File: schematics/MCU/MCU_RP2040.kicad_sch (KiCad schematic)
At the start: 34 parts, among them X1 ECS-2520MVLC-120-CN

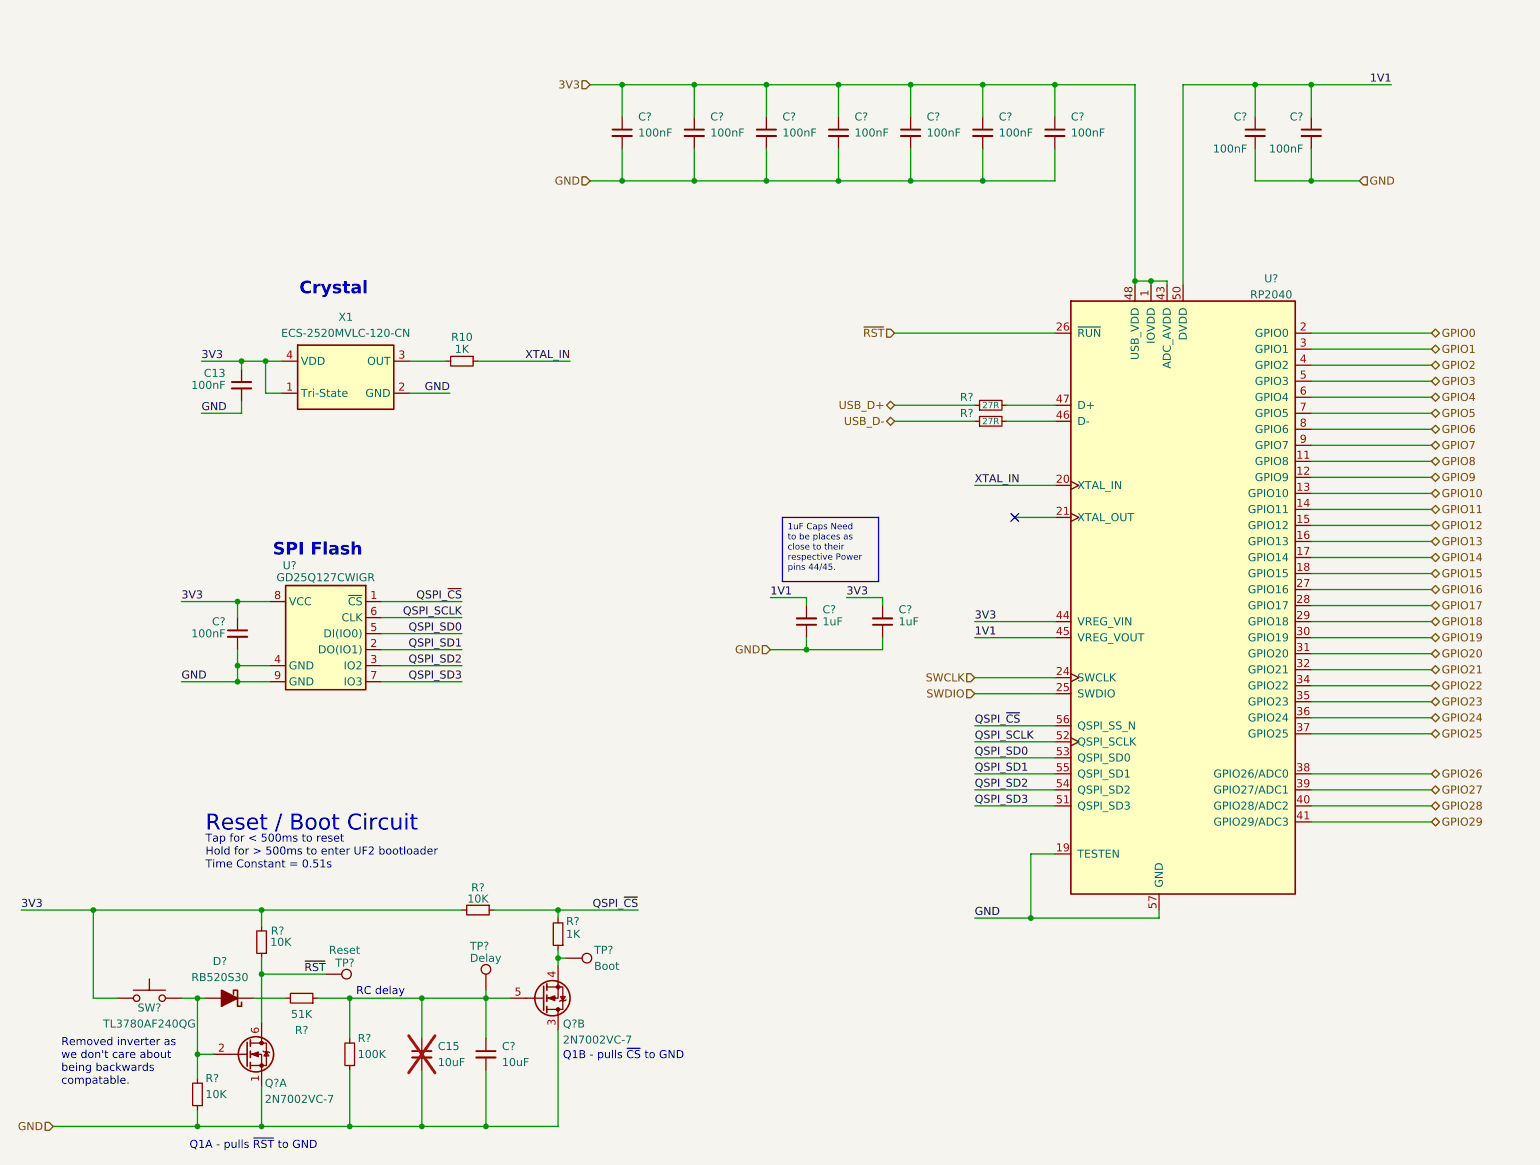
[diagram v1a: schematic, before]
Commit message: Cleanup design blocks, add bq240xx
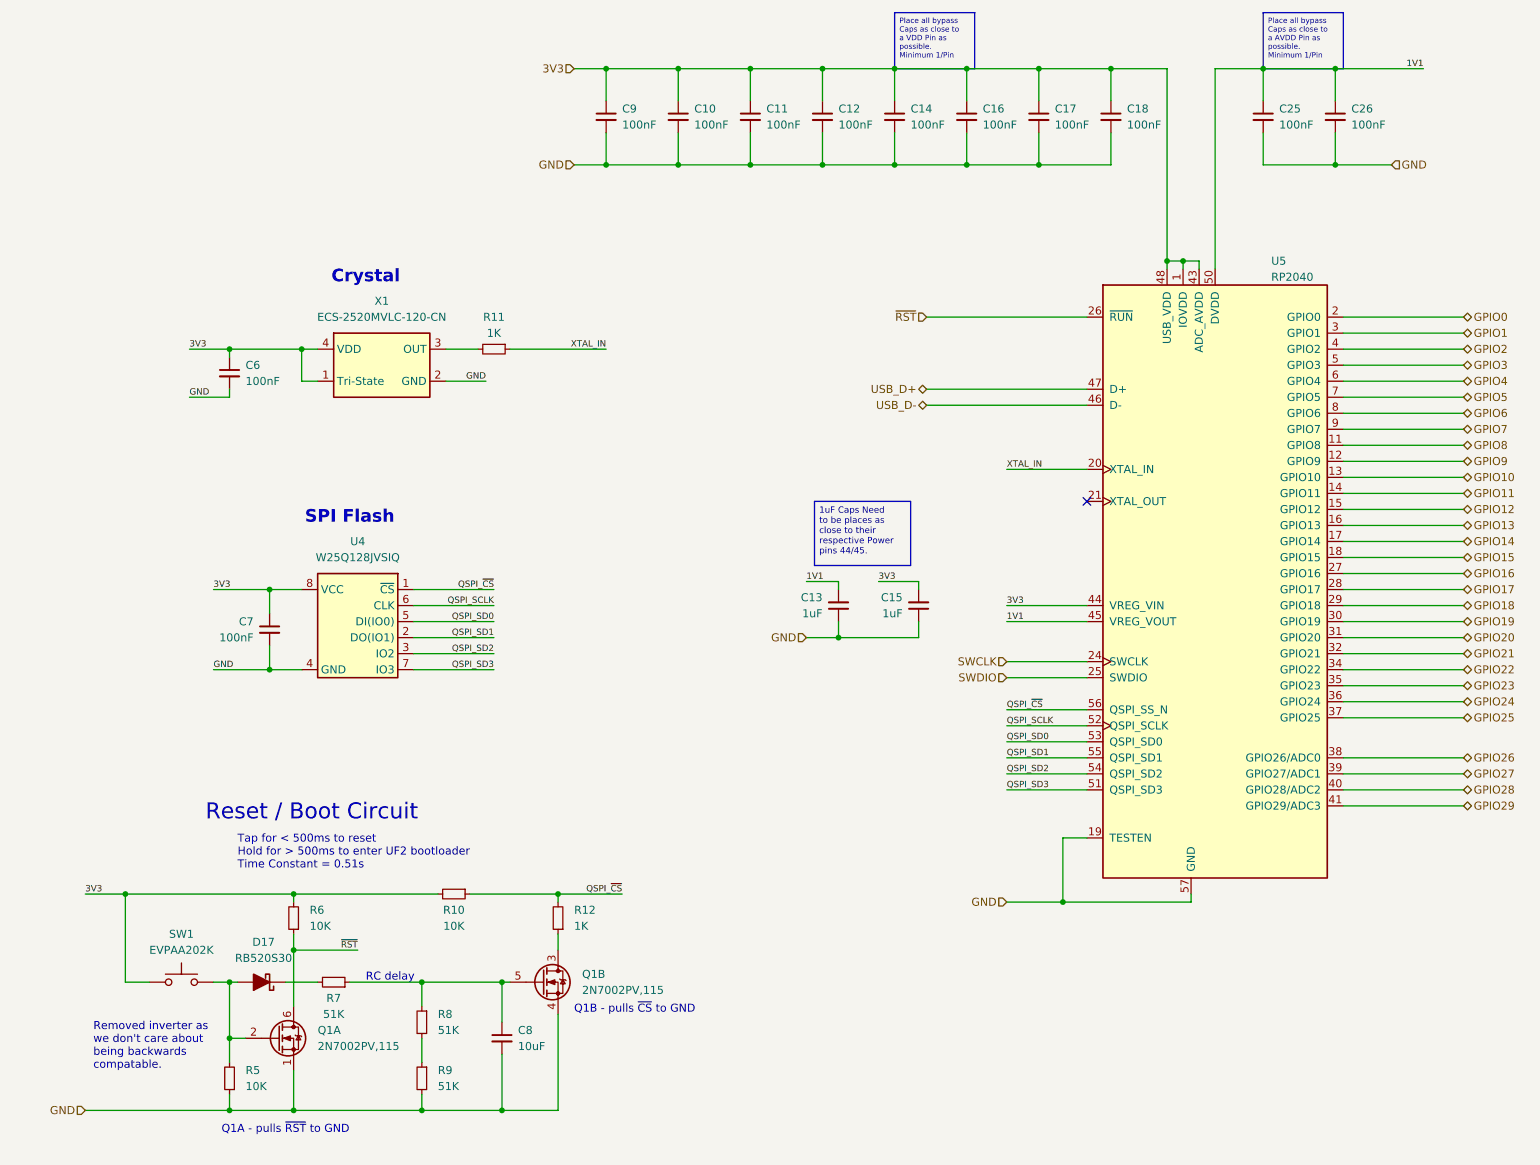
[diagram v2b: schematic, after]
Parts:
- removed C15: 10uF, Capacitor_SMD:C_0805_2012Metric, symbol Device:C_Small
- removed C? (x2): 100nF, Capacitor_SMD:C_0402_1005Metric, symbol Device:C_Small
- removed Q?: 2N7002VC-7, Package_TO_SOT_SMD:SOT-363_SC-70-6, symbol Transistor_FET:FDG6335N
- removed R?: 100K, Resistor_SMD:R_0402_1005Metric, symbol Device:R_Small
- removed R? (x2): 27R, Resistor_SMD:R_0402_1005Metric, symbol Device:R_Small
- removed TP?: Delay, TestPoint:TestPoint_Pad_D1.0mm, symbol Connector:TestPoint
- removed TP?: Boot, TestPoint:TestPoint_Pad_D1.0mm, symbol Connector:TestPoint
- removed TP?: Reset, TestPoint:TestPoint_Pad_D1.0mm, symbol Connector:TestPoint
- added C18, C25, C26: 100nF, Capacitor_SMD:C_0603_1608Metric, symbol Device:C_Small
- added unit 1 of Q1
- added R8, R9: 51K, Resistor_SMD:R_0603_1608Metric, symbol Device:R_Small
- C10, C11, C12, C14, C16, C17, C7, C9: renamed from C?; footprint Capacitor_SMD:C_0402_1005Metric -> Capacitor_SMD:C_0603_1608Metric; LCSC (none) -> C432917; MPN CC0402KPX7R9BB104 -> CC0603KPX7R9BB104; Price $0.17 -> $0.10; Rating CAP 0402 50V 100 NF X7R -> CAP CER 0.1UF 50V X7R 0603; Supplier PN 13-CC0402KPX7R9BB104CT-ND -> (none); digikey (none) -> 311-3567-1-ND; mouser (none) -> 603-CC603KPX7R9BB104
- C13, C15: renamed from C?; LCSC (none) -> C14664; Supplier PN 311-1445-1-ND -> (none); digikey (none) -> 311-1445-1-ND; mouser (none) -> 603-CC603KRX5R8BB105
- C6: renamed from C13; footprint Capacitor_SMD:C_0402_1005Metric -> Capacitor_SMD:C_0603_1608Metric; LCSC (none) -> C432917; MPN CC0402KPX7R9BB104 -> CC0603KPX7R9BB104; Price $0.17 -> $0.10; Rating CAP 0402 50V 100 NF X7R -> CAP CER 0.1UF 50V X7R 0603; Supplier PN 13-CC0402KPX7R9BB104CT-ND -> (none); digikey (none) -> 311-3567-1-ND; mouser (none) -> 603-CC603KPX7R9BB104
- C8: renamed from C?; LCSC (none) -> C2932476; Supplier PN 311-1869-1-ND -> (none); digikey (none) -> 311-1869-1-ND; mouser (none) -> 603-CC805KKX5R8BB106
- D17: renamed from D?; symbol PCM_Diode_Schottky_AKL:RB520S30 -> Mad_Symbols:RB520S30; LCSC (none) -> C232575; Price $0.21 -> $0.21; Supplier PN RB520S30T5GOSCT-ND -> (none); digikey (none) -> RB520S30T5GOSCT-ND; mouser (none) -> 863-RB520S30T5G
- Q1: renamed from Q?; value 2N7002VC-7 -> 2N7002PV,115; footprint Package_TO_SOT_SMD:SOT-363_SC-70-6 -> Package_TO_SOT_SMD:SOT-666; LCSC (none) -> C551422; MPN 2N7002VC-7 -> 2N7002PV,115; Price $0.64 -> $0.64; Rating MOSFET 2N-CH 60V 0.28A SOT563 -> MOSFET 2N-CH 60V 0.35A SOT666; Supplier PN 2N7002VC-7DICT-ND -> (none); digikey (none) -> 1727-4792-1-ND; mouser (none) -> 771-2N7002PV-115
- R10, R5, R6: renamed from R?; footprint Resistor_SMD:R_0402_1005Metric -> Resistor_SMD:R_0603_1608Metric; LCSC (none) -> C60490; MPN RC0402FR-0710KL -> RC0603FR-0710KL; Price $0.16 -> $0.10; Rating RES 10K OHM 1% 1/16W 0402 -> RES 10K OHM 1% 1/16W 0603; Supplier PN 311-10.0KLRCT-ND -> (none); digikey (none) -> 311-10.0KHRCT-ND; mouser (none) -> 603-RC0603FR-0710KL
- R11: renamed from R10; footprint Resistor_SMD:R_0402_1005Metric -> Resistor_SMD:R_0603_1608Metric; LCSC (none) -> C106235; MPN RC0402FR-071KL -> RC0603FR-071KL; Price $0.16 -> $0.10; Rating RES 1K OHM 1% 1/16W 0402 -> RES 1K OHM 1% 1/16W 0603; Supplier PN 311-1.00KLRCT-ND -> (none); digikey (none) -> 311-1.00KHRCT-ND; mouser (none) -> 603-RC0603FR-071KL
- R12: renamed from R?; footprint Resistor_SMD:R_0402_1005Metric -> Resistor_SMD:R_0603_1608Metric; LCSC (none) -> C106235; MPN RC0402FR-071KL -> RC0603FR-071KL; Price $0.16 -> $0.10; Rating RES 1K OHM 1% 1/16W 0402 -> RES 1K OHM 1% 1/16W 0603; Supplier PN 311-1.00KLRCT-ND -> (none); digikey (none) -> 311-1.00KHRCT-ND; mouser (none) -> 603-RC0603FR-071KL
- R7: renamed from R?; footprint Resistor_SMD:R_0402_1005Metric -> Resistor_SMD:R_0603_1608Metric; LCSC (none) -> C107229; MPN RC0402FR-0751KL -> RC0603FR-0751KL; Price $0.16 -> $0.10; Rating RES 51K OHM 1% 1/16W 0402 -> RES 51K OHM 1% 1/16W 0603; Supplier PN 311-51.0KLRCT-ND -> (none); digikey (none) -> 311-51.0KHRCT-ND; mouser (none) -> 603-RC0603FR-0751KL
- SW1: renamed from SW?; value TL3780AF240QG -> EVPAA202K; footprint Mad_Footprints:SW_TL3780AF240QG -> Mad_Footprints:EVP-AA202K; LCSC (none) -> C79147; MPN TL3780AF240QG -> EVPAA202K; Manufacturer E-Switch -> Panasonic Electronic Components; Price $0.41 -> $1.26; Rating SWITCH TACTILE SPST-NO 0.05A 12V -> SWITCH TACTILE SPST-NO 0.02A 15V; Supplier PN EG5393CT-ND -> (none); digikey (none) -> P13348SCT-ND; mouser (none) -> 667-EVP-AA202K
- U4: renamed from U?; value GD25Q127CWIGR -> W25Q128JVSIQ; footprint Mad_Footprints:GD25LQ128DYIGR -> Mad_Footprints:SOIC-8_5.23x5.23mm_P1.27mm; LCSC (none) -> C97521; MPN GD25Q127CWIGR -> W25Q128JVSIQ; Manufacturer GigaDevice Semiconductor (HK) Limited -> Winbond Electronics; Price $3.48 -> $2.72; Rating IC FLASH 128MBIT SPI/QUAD 8WSON -> IC FLASH 128MBIT SPI/QUAD 8SOIC; Supplier PN 1970-1048-1-ND -> (none); digikey (none) -> W25Q128JVSIQ-ND
- U5: renamed from U?; LCSC (none) -> C2040; Price $1.11 -> $1.11; Supplier PN 2648-SC0914(13)CT-ND -> (none); digikey (none) -> 2648-SC0914(13)CT-ND; mouser (none) -> 358-SC091413
- X1: footprint Mad_Footprints:Crystal_SMD_ECX-32-4Pin_3.2x2.5mm -> Oscillator:Oscillator_SMD_ECS_2520MV-xxx-xx-4Pin_2.5x2.0mm; symbol Mad_Symbols:ECS-2520MV-xxx-xx -> Mad_Symbols:ECS-2520MV; LCSC (none) -> C669073; Supplier PN 50-ECS-2520MVLC-120-CN-TRCT-ND -> (none); digikey (none) -> 50-ECS-2520MVLC-120-CN-TRCT-ND; mouser (none) -> 520-2520MVLC-120CNTR
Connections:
- net 1V1: now also C25.1, C26.1
- net 3V3: now also SW1.1, C18.1; no longer SW1.2
- net GND: now also Q1.4 (S), C18.2, C25.2, C26.2, Q1.1 (S), R9.2; no longer Q1.3 (D), U4.9 (GND)
- net USB_D+: now also U5.47 (D+)
- net USB_D-: now also U5.46 (D-)
- net ~{RST}: now also Q1.6 (D)
- net at C8.1, Q1.5 (G), R7.1: now also R8.1
- net at R12.1: now also Q1.3 (D); no longer Q1.4 (S)
- net at D17.2 (A), R5.2: now also SW1.2, Q1.2 (G); no longer SW1.1
- new net: R8.2, R9.1
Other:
- moved on the sheet: C10, C11, C12, C13, C14, C15, C16, C17, C6, C7, C8, C9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

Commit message: Update lib, embed models into footprints and remove from models folder
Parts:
- C10, C11, C12, C14, C16, C17, C18, C25, C26, C6, C7, C9, R10, R11, R12, R5, R6, R7, R8, R9: Price $0.10 -> $0.10
- C8: Supplier PN (none) -> 311-1869-1-ND
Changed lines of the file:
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@@
 			)
 		)
-		(property "Price" "$0.10 "
+		(property "Price" "$0.10"
 			(at 147.32 33.02 0)
 			(effects
@@
 			)
 		)
-		(property "Price" "$0.10 "
+		(property "Price" "$0.10"
 			(at 63.5 160.02 0)
 			(effects
@@
 			)
 		)
-		(property "Price" "$0.10 "
+		(property "Price" "$0.10"
 			(at 53.34 185.42 0)
 			(effects
@@
 			)
 		)
+		(property "Supplier PN" "311-1869-1-ND"
+			(at 96.52 179.07 0)
+			(effects
+				(font
+					(size 1.27 1.27)
+				)
+				(hide yes)
+			)
+		)
 		(pin "2"
 		)
@@
 			)
 		)
-		(property "Price" "$0.10 "
+		(property "Price" "$0.10"
 			(at 113.03 33.02 0)
 			(effects
@@
 			)
 		)
-		(property "Price" "$0.10 "
+		(property "Price" "$0.10"
 			(at 124.46 33.02 0)
 			(effects
@@
 			)
 		)
-		(property "Price" "$0.10 "
+		(property "Price" "$0.10"
 			(at 59.69 114.3 0)
 			(effects
@@
 			)
 		)
-		(property "Price" "$0.10 "
+		(property "Price" "$0.10"
 			(at 158.75 33.02 0)
 			(effects
@@
 			)
 		)
-		(property "Price" "$0.10 "
+		(property "Price" "$0.10"
 			(at 228.6 33.02 0)
 			(effects
@@
 			)
 		)
-		(property "Price" "$0.10 "
+		(property "Price" "$0.10"
 			(at 83.82 185.42 0)
 			(effects
@@
 			)
 		)
-		(property "Price" "$0.10 "
+		(property "Price" "$0.10"
 			(at 53.34 73.66 0)
 			(effects
@@
 			)
 		)
-		(property "Price" "$0.10 "
+		(property "Price" "$0.10"
 			(at 170.18 33.02 0)
 			(effects
@@
 			)
 		)
-		(property "Price" "$0.10 "
+		(property "Price" "$0.10"
 			(at 135.89 33.02 0)
 			(effects
@@
 			)
 		)
-		(property "Price" "$0.10 "
+		(property "Price" "$0.10"
 			(at 105.41 160.02 0)
 			(effects
@@
 			)
 		)
-		(property "Price" "$0.10 "
+		(property "Price" "$0.10"
 			(at 69.85 170.18 0)
 			(effects
@@
 			)
 		)
-		(property "Price" "$0.10 "
+		(property "Price" "$0.10"
 			(at 217.17 33.02 0)
 			(effects
@@
 			)
 		)
-		(property "Price" "$0.10 "
+		(property "Price" "$0.10"
 			(at 193.04 33.02 0)
 			(effects
@@
 			)
 		)
-		(property "Price" "$0.10 "
+		(property "Price" "$0.10"
 			(at 83.82 176.53 0)
 			(effects
@@
 			)
 		)
-		(property "Price" "$0.10 "
+		(property "Price" "$0.10"
 			(at 88.9 156.21 0)
 			(effects
@@
 			)
 		)
-		(property "Price" "$0.10 "
+		(property "Price" "$0.10"
 			(at 95.25 69.85 0)
 			(effects
@@
 			)
 		)
-		(property "Price" "$0.10 "
+		(property "Price" "$0.10"
 			(at 181.61 33.02 0)
 			(effects
